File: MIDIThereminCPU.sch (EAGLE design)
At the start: 57 parts, among them IC1 UA78M05DCY, IC2 74AHC1G04DCK, IC3 74AHC1G04DCK, J1 DCJ0202, Q1 16MHz, U1 ATMEGA328P-AU

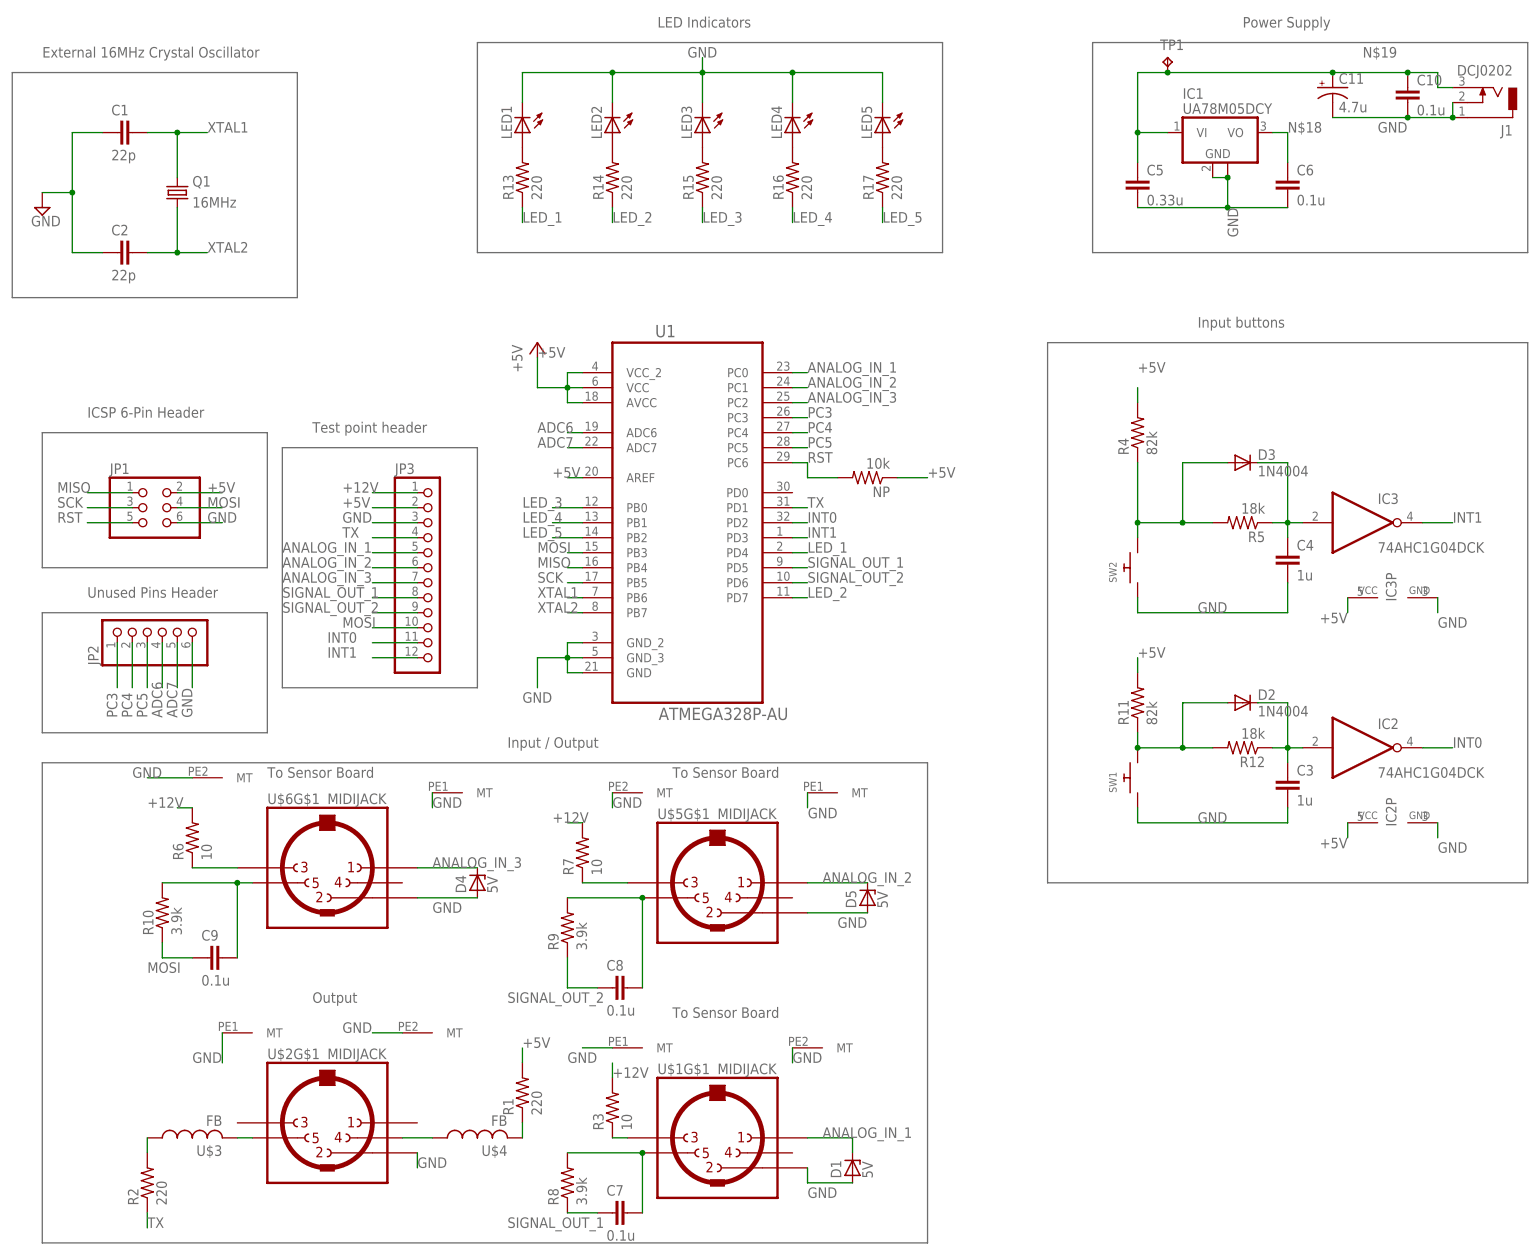
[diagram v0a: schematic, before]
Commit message: Drew connections
Drew in the connections. These look horrible and only connect to labeled points on the arduino, so I don't see the point but oh well.
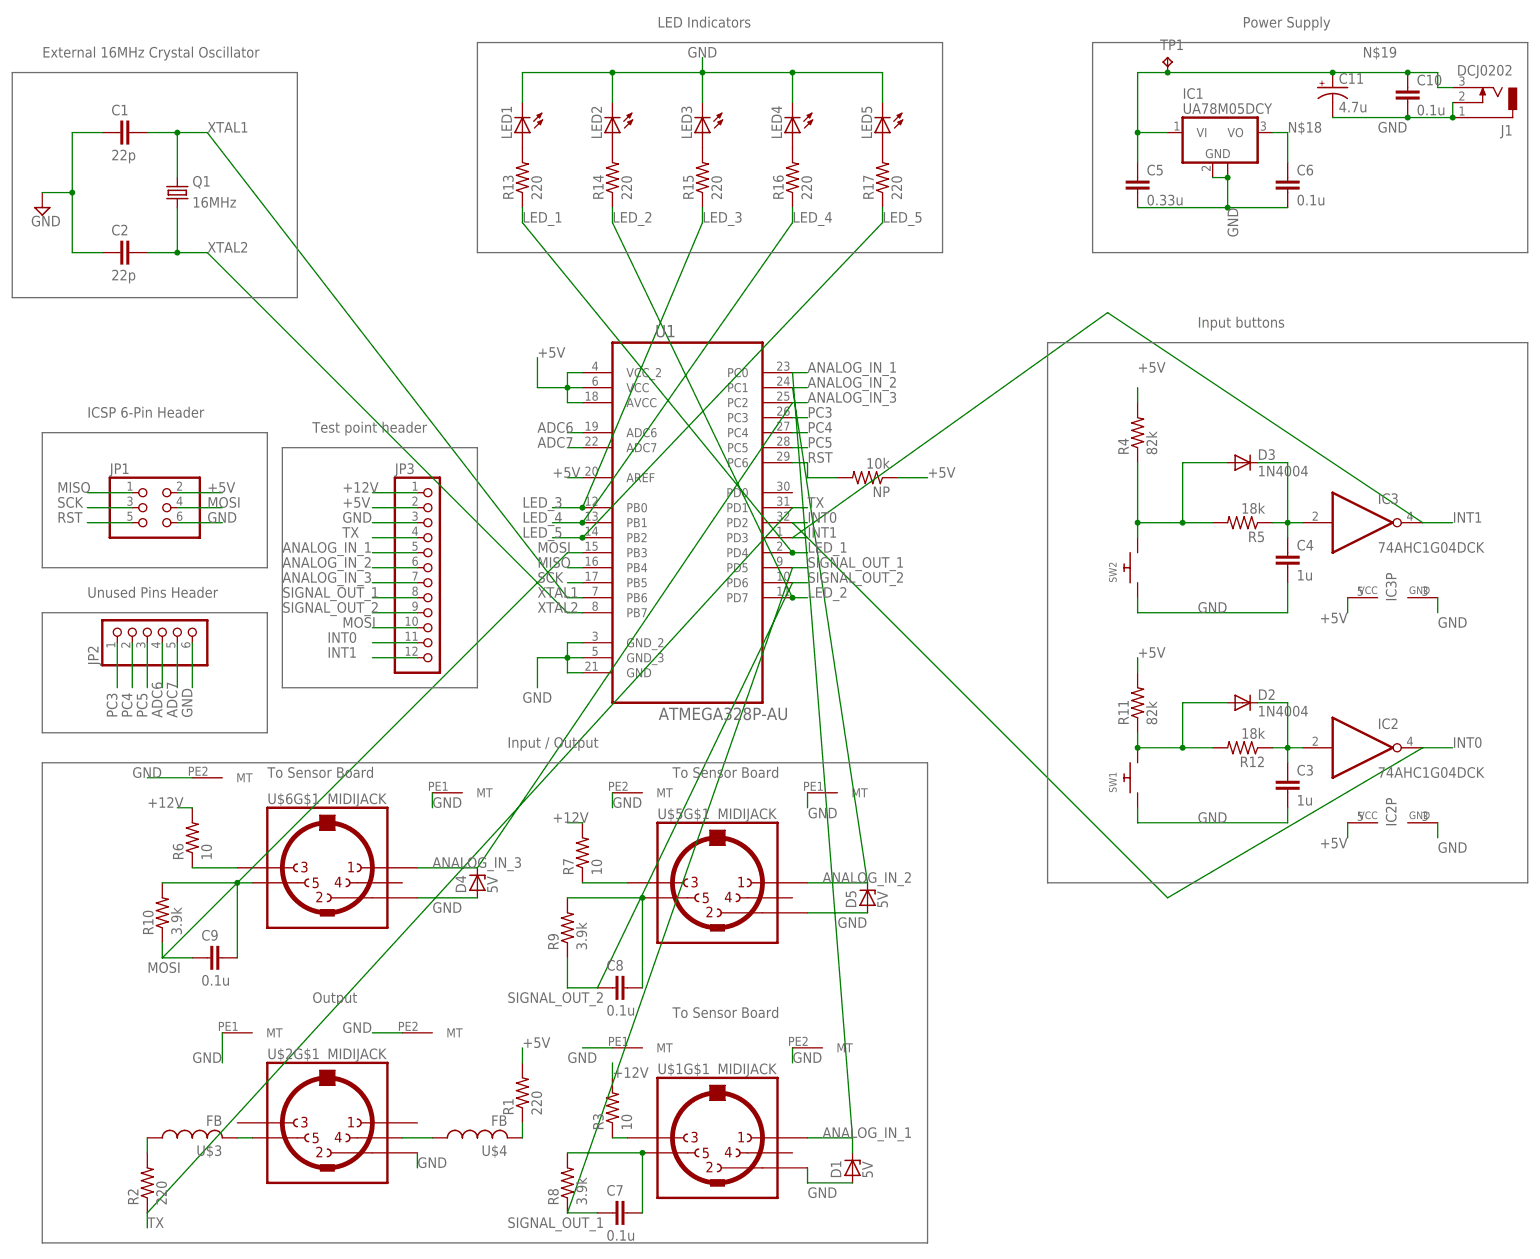
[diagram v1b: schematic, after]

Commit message: Add files via upload
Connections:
- removed net N$18: C6.1, IC1.VO
- removed net N$19: C10.1, C11.+, C5.1, IC1.VI, J1.3, TP1.TP
- net +12V: now also C10.1, C11.+, C5.1, IC1.VI, J1.3, TP1.TP
- net +5V: now also C6.1, IC1.VO
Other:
- moved on the sheet: NP

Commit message: Add files via upload
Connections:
- net GND: now also C7.1, C8.1, C9.1
- net MOSI: no longer C9.1
- net SIGNAL_OUT_1: no longer C7.1
- net SIGNAL_OUT_2: no longer C8.1
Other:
- moved on the sheet: C7, C8, C9, R8
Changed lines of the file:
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@@
 <part name="GND23" library="supply1" deviceset="GND" device=""/>
 <part name="P+16" library="supply1" deviceset="+12V" device=""/>
+<part name="GND24" library="supply1" deviceset="GND" device=""/>
+<part name="GND25" library="supply1" deviceset="GND" device=""/>
+<part name="GND26" library="supply1" deviceset="GND" device=""/>
 </parts>
 <sheets>
@@
 <instance part="D5" gate="G$1" x="160.02" y="58.42" rot="R90"/>
 <instance part="R7" gate="G$1" x="111.76" y="66.04" rot="R90"/>
-<instance part="R8" gate="G$1" x="109.22" y="10.16" rot="R90"/>
-<instance part="C7" gate="G$1" x="116.84" y="5.08" smashed="yes" rot="R90">
-<attribute name="NAME" x="115.824" y="8.001" size="1.778" layer="95"/>
-<attribute name="VALUE" x="115.824" y="0.381" size="1.778" layer="96"/>
+<instance part="R8" gate="G$1" x="109.22" y="15.24"/>
+<instance part="C7" gate="G$1" x="116.84" y="10.16" smashed="yes" rot="R180">
+<attribute name="NAME" x="113.919" y="9.144" size="1.778" layer="95" rot="R90"/>
+<attribute name="VALUE" x="121.539" y="9.144" size="1.778" layer="96" rot="R90"/>
 </instance>
 <instance part="R9" gate="G$1" x="109.22" y="53.34" rot="R90"/>
-<instance part="C8" gate="G$1" x="116.84" y="43.18" smashed="yes" rot="R90">
-<attribute name="NAME" x="115.824" y="46.101" size="1.778" layer="95"/>
-<attribute name="VALUE" x="115.824" y="38.481" size="1.778" layer="96"/>
+<instance part="C8" gate="G$1" x="116.84" y="53.34" smashed="yes" rot="R180">
+<attribute name="NAME" x="113.919" y="52.324" size="1.778" layer="95" rot="R90"/>
+<attribute name="VALUE" x="121.539" y="52.324" size="1.778" layer="96" rot="R90"/>
 </instance>
 <instance part="R10" gate="G$1" x="40.64" y="55.88" rot="R90"/>
-<instance part="C9" gate="G$1" x="48.26" y="48.26" smashed="yes" rot="R90">
-<attribute name="NAME" x="47.244" y="51.181" size="1.778" layer="95"/>
-<attribute name="VALUE" x="47.244" y="43.561" size="1.778" layer="96"/>
+<instance part="C9" gate="G$1" x="48.26" y="55.88" smashed="yes" rot="R180">
+<attribute name="NAME" x="45.339" y="54.864" size="1.778" layer="95" rot="R90"/>
+<attribute name="VALUE" x="52.959" y="54.864" size="1.778" layer="96" rot="R90"/>
 </instance>
 <instance part="LED1" gate="G$1" x="101.6" y="187.96" rot="R180"/>
@@
 </instance>
 <instance part="P+16" gate="1" x="76.2" y="132.08"/>
+<instance part="GND24" gate="1" x="116.84" y="5.08"/>
+<instance part="GND25" gate="1" x="116.84" y="48.26"/>
+<instance part="GND26" gate="1" x="48.26" y="50.8"/>
 </instances>
 <busses>
@@
 <pinref part="U$5" gate="G$5" pin="MT"/>
 </segment>
+<segment>
+<pinref part="C7" gate="G$1" pin="1"/>
+<pinref part="GND24" gate="1" pin="GND"/>
+</segment>
+<segment>
+<pinref part="C8" gate="G$1" pin="1"/>
+<pinref part="GND25" gate="1" pin="GND"/>
+</segment>
+<segment>
+<pinref part="C9" gate="G$1" pin="1"/>
+<pinref part="GND26" gate="1" pin="GND"/>
+</segment>
 </net>
 <net name="MISO" class="0">
@@
 </segment>
 <segment>
-<pinref part="C9" gate="G$1" pin="1"/>
-<wire x1="45.72" y1="48.26" x2="40.64" y2="48.26" width="0.1524" layer="91"/>
 <pinref part="R10" gate="G$1" pin="1"/>
 <wire x1="40.64" y1="48.26" x2="40.64" y2="50.8" width="0.1524" layer="91"/>
@@
 <segment>
 <pinref part="R8" gate="G$1" pin="1"/>
-<pinref part="C7" gate="G$1" pin="1"/>
-<wire x1="109.22" y1="5.08" x2="114.3" y2="5.08" width="0.1524" layer="91"/>
-<label x="99.06" y="2.54" size="1.778" layer="95"/>
+<wire x1="104.14" y1="15.24" x2="104.14" y2="10.16" width="0.1524" layer="91"/>
+<label x="91.44" y="7.62" size="1.778" layer="95"/>
 </segment>
 <segment>
@@
 <pinref part="R10" gate="G$1" pin="2"/>
 <pinref part="U$6" gate="G$1" pin="5"/>
-<wire x1="40.64" y1="60.96" x2="53.34" y2="60.96" width="0.1524" layer="91"/>
+<wire x1="40.64" y1="60.96" x2="48.26" y2="60.96" width="0.1524" layer="91"/>
 <pinref part="C9" gate="G$1" pin="2"/>
-<wire x1="53.34" y1="60.96" x2="55.88" y2="60.96" width="0.1524" layer="91"/>
-<wire x1="53.34" y1="48.26" x2="53.34" y2="60.96" width="0.1524" layer="91"/>
-<junction x="53.34" y="60.96"/>
+<wire x1="48.26" y1="60.96" x2="55.88" y2="60.96" width="0.1524" layer="91"/>
+<junction x="48.26" y="60.96"/>
 </segment>
 </net>
@@
 <pinref part="R9" gate="G$1" pin="2"/>
 <pinref part="U$5" gate="G$1" pin="5"/>
-<wire x1="109.22" y1="58.42" x2="121.92" y2="58.42" width="0.1524" layer="91"/>
+<wire x1="109.22" y1="58.42" x2="116.84" y2="58.42" width="0.1524" layer="91"/>
 <pinref part="C8" gate="G$1" pin="2"/>
-<wire x1="121.92" y1="43.18" x2="121.92" y2="58.42" width="0.1524" layer="91"/>
-<junction x="121.92" y="58.42"/>
+<wire x1="116.84" y1="58.42" x2="121.92" y2="58.42" width="0.1524" layer="91"/>
+<junction x="116.84" y="58.42"/>
 </segment>
 </net>
 <net name="SIGNAL_OUT_2" class="0">
 <segment>
-<pinref part="C8" gate="G$1" pin="1"/>
-<wire x1="114.3" y1="43.18" x2="109.22" y2="43.18" width="0.1524" layer="91"/>
 <pinref part="R9" gate="G$1" pin="1"/>
 <wire x1="109.22" y1="43.18" x2="109.22" y2="48.26" width="0.1524" layer="91"/>
@@
 <pinref part="R8" gate="G$1" pin="2"/>
 <pinref part="U$1" gate="G$1" pin="5"/>
-<wire x1="109.22" y1="15.24" x2="121.92" y2="15.24" width="0.1524" layer="91"/>
+<wire x1="114.3" y1="15.24" x2="121.92" y2="15.24" width="0.1524" layer="91"/>
 <pinref part="C7" gate="G$1" pin="2"/>
-<wire x1="121.92" y1="5.08" x2="121.92" y2="15.24" width="0.1524" layer="91"/>
-<junction x="121.92" y="15.24"/>
-</segment>
-</net>
+<wire x1="116.84" y1="15.24" x2="121.92" y2="15.24" width="0.1524" layer="91"/>
+</segment>
+</net>
